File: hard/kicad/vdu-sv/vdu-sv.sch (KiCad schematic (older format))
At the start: 36 parts, among them J1 IOx, J2 (S)VGA, J3 IOx, U1 74HC138, U10 74HC245, U11 74HC245, U12 74HC245, U13 74HC574, U14 74HC157, U15 74HC86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

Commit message: first definitive placement
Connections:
- net D_BL: now also U10.12 (B6); no longer U10.11 (B7)
- net D_GH: now also U10.17 (B1); no longer U10.18 (B0)
- net D_RH: now also U10.18 (B0); no longer U10.17 (B1)
- net D_RL: now also U10.11 (B7); no longer U10.12 (B6)
- net I_BL: now also U10.8 (A6), U21.6; no longer U10.9 (A7), U21.11
- net I_GH: now also U10.3 (A1); no longer U10.2 (A0)
- net I_GL: now also U21.11; no longer U21.6
- net I_RH: now also U10.2 (A0); no longer U10.3 (A1)
- net I_RL: now also U10.9 (A7); no longer U10.8 (A6)
- net X_BL: now also U21.4; no longer U21.12
- net X_GL: now also U21.12; no longer U21.4
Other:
- moved on the sheet: R1, R2, R22, R23, U21B, U21D
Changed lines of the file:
@@
 L 74xx:74HC86 U21
 U 4 1 65C4FD1C
-P 7300 6100
-F 0 "U21" V 7325 6100 50  0000 C CNN
-F 1 "74HC86" V 7225 6100 50  0000 C CNN
-F 2 "Package_DIP:DIP-14_W7.62mm_Socket" H 7300 6100 50  0001 C CNN
-F 3 "http://www.ti.com/lit/gpn/sn74HC86" H 7300 6100 50  0001 C CNN
-	4    7300 6100
+P 6600 6100
+F 0 "U21" V 6625 6100 50  0000 C CNN
+F 1 "74HC86" V 6525 6100 50  0000 C CNN
+F 2 "Package_DIP:DIP-14_W7.62mm_Socket" H 6600 6100 50  0001 C CNN
+F 3 "http://www.ti.com/lit/gpn/sn74HC86" H 6600 6100 50  0001 C CNN
+	4    6600 6100
 	0    -1   -1   0
 $EndComp
@@
 L 74xx:74HC86 U21
 U 2 1 65C4FD30
-P 6600 6100
-F 0 "U21" V 6625 6100 50  0000 C CNN
-F 1 "74HC86" V 6525 6100 50  0000 C CNN
-F 2 "Package_DIP:DIP-14_W7.62mm_Socket" H 6600 6100 50  0001 C CNN
-F 3 "http://www.ti.com/lit/gpn/sn74HC86" H 6600 6100 50  0001 C CNN
-	2    6600 6100
-	0    -1   -1   0
-$EndComp
-Wire Wire Line
-	9100 5800 7300 5800
+P 7300 6100
+F 0 "U21" V 7325 6100 50  0000 C CNN
+F 1 "74HC86" V 7225 6100 50  0000 C CNN
+F 2 "Package_DIP:DIP-14_W7.62mm_Socket" H 7300 6100 50  0001 C CNN
+F 3 "http://www.ti.com/lit/gpn/sn74HC86" H 7300 6100 50  0001 C CNN
+	2    7300 6100
+	0    -1   -1   0
+$EndComp
 Wire Wire Line
 	6350 6400 6350 6425
@@
 	5850 6400 5850 6625
 Wire Wire Line
-	9100 5700 6950 5700
+	9100 5700 7300 5700
 Wire Wire Line
 	9100 5600 6600 5600
@@
 	9100 5300 7300 5300
 Wire Wire Line
-	9100 5200 6950 5200
-Wire Wire Line
-	9100 5100 6600 5100
+	9100 5200 6600 5200
+Wire Wire Line
+	9100 5100 6950 5100
 Wire Wire Line
 	10100 5800 10300 5800
@@
 L Device:R R23
 U 1 1 65F219EF
+P 10450 5700
+F 0 "R23" V 10400 5875 50  0000 C CNN
+F 1 "1K" V 10450 5700 50  0000 C CNN
+F 2 "Resistor_THT:R_Axial_DIN0207_L6.3mm_D2.5mm_P2.54mm_Vertical" V 10380 5700 50  0001 C CNN
+F 3 "~" H 10450 5700 50  0001 C CNN
+	1    10450 5700
+	0    1    1    0
+$EndComp
+$Comp
+L Device:R R22
+U 1 1 65F1EFAB
 P 10450 5800
-F 0 "R23" V 10400 5975 50  0000 C CNN
-F 1 "1K" V 10450 5800 50  0000 C CNN
+F 0 "R22" V 10400 5975 50  0000 C CNN
+F 1 "2K2" V 10450 5800 50  0000 C CNN
 F 2 "Resistor_THT:R_Axial_DIN0207_L6.3mm_D2.5mm_P2.54mm_Vertical" V 10380 5800 50  0001 C CNN
 F 3 "~" H 10450 5800 50  0001 C CNN
 	1    10450 5800
-	0    1    1    0
-$EndComp
-$Comp
-L Device:R R22
-U 1 1 65F1EFAB
-P 10450 5700
-F 0 "R22" V 10400 5875 50  0000 C CNN
-F 1 "2K2" V 10450 5700 50  0000 C CNN
-F 2 "Resistor_THT:R_Axial_DIN0207_L6.3mm_D2.5mm_P2.54mm_Vertical" V 10380 5700 50  0001 C CNN
-F 3 "~" H 10450 5700 50  0001 C CNN
-	1    10450 5700
 	0    1    1    0
 $EndComp
@@
 	0    1    1    0
 $EndComp
+Text Label 10125 5700 0    50   ~ 0
+D_BL
 Text Label 10125 5800 0    50   ~ 0
-D_BL
-Text Label 10125 5700 0    50   ~ 0
 D_RL
 Text Label 10125 5600 0    50   ~ 0
@@
 	10625 6400 10625 5900
 Wire Wire Line
-	10300 5200 10100 5200
+	10300 5100 10100 5100
 Wire Wire Line
 	10300 5300 10100 5300
 Text Label 10125 5300 0    50   ~ 0
 D_GM
-Text Label 10125 5200 0    50   ~ 0
+Text Label 10125 5100 0    50   ~ 0
 D_RH
 $Comp
@@
 L Device:R R1
 U 1 1 65AA0EB0
-P 10450 5200
-F 0 "R1" V 10400 5350 50  0000 C CNN
-F 1 "680" V 10450 5200 50  0000 C CIN
-F 2 "Resistor_THT:R_Axial_DIN0207_L6.3mm_D2.5mm_P2.54mm_Vertical" V 10380 5200 50  0001 C CNN
-F 3 "~" H 10450 5200 50  0001 C CNN
-	1    10450 5200
+P 10450 5100
+F 0 "R1" V 10400 5250 50  0000 C CNN
+F 1 "680" V 10450 5100 50  0000 C CIN
+F 2 "Resistor_THT:R_Axial_DIN0207_L6.3mm_D2.5mm_P2.54mm_Vertical" V 10380 5100 50  0001 C CNN
+F 3 "~" H 10450 5100 50  0001 C CNN
+	1    10450 5100
 	0    1    1    0
 $EndComp
@@
 	0    1    1    0
 $EndComp
-Text Label 10125 5100 0    50   ~ 0
+Text Label 10125 5200 0    50   ~ 0
 D_GH
 Wire Wire Line
-	10100 5100 10300 5100
+	10100 5200 10300 5200
 $Comp
 L Device:R R2
 U 1 1 65AA38B7
-P 10450 5100
-F 0 "R2" V 10400 5250 50  0000 C CNN
-F 1 "680" V 10450 5100 50  0000 C CNN
-F 2 "Resistor_THT:R_Axial_DIN0207_L6.3mm_D2.5mm_P2.54mm_Vertical" V 10380 5100 50  0001 C CNN
-F 3 "~" H 10450 5100 50  0001 C CNN
-	1    10450 5100
-	0    1    1    0
-$EndComp
-Wire Wire Line
-	10800 5800 10600 5800
-Wire Wire Line
-	10600 5700 10700 5700
+P 10450 5200
+F 0 "R2" V 10400 5350 50  0000 C CNN
+F 1 "680" V 10450 5200 50  0000 C CNN
+F 2 "Resistor_THT:R_Axial_DIN0207_L6.3mm_D2.5mm_P2.54mm_Vertical" V 10380 5200 50  0001 C CNN
+F 3 "~" H 10450 5200 50  0001 C CNN
+	1    10450 5200
+	0    1    1    0
+$EndComp
 Wire Wire Line
 	10600 5600 10750 5600
@@
 	10600 5300 10750 5300
 Wire Wire Line
-	10600 5200 10700 5200
-Wire Wire Line
 	10700 5000 10900 5000
 Wire Wire Line
 	10800 5200 10900 5200
 Wire Wire Line
-	10800 5400 10800 5800
-Connection ~ 10800 5400
-Wire Wire Line
 	10800 5400 10800 5200
 Wire Wire Line
-	10700 5700 10700 5500
-Connection ~ 10700 5500
-Wire Wire Line
-	10700 5500 10700 5200
-Wire Wire Line
 	10750 5600 10750 5300
-Wire Wire Line
-	10750 5100 10900 5100
-Wire Wire Line
-	10600 5100 10750 5100
-Connection ~ 10750 5100
 Connection ~ 10750 5300
 Wire Wire Line
-	10750 5300 10750 5100
-Connection ~ 10700 5200
-Wire Wire Line
-	10700 5200 10700 5000
-Wire Wire Line
-	6950 5700 6950 5800
+	10750 5300 10750 5200
 Wire Wire Line
 	6600 5600 6600 5800
@@
 	6250 5500 6250 5800
 Wire Wire Line
-	6600 5100 6600 4925
-Wire Wire Line
-	6950 4925 6950 5200
-Wire Wire Line
 	7300 5300 7300 4925
 Wire Wire Line
 	7650 4925 7650 5400
+Text Label 9100 5700 2    50   ~ 0
+I_BL
 Text Label 9100 5800 2    50   ~ 0
-I_BL
-Text Label 9100 5700 2    50   ~ 0
 I_RL
 Text Label 9100 5600 2    50   ~ 0
@@
 Text Label 9100 5400 2    50   ~ 0
 I_BH
+Text Label 9100 5100 2    50   ~ 0
+I_RH
 Text Label 9100 5200 2    50   ~ 0
-I_RH
-Text Label 9100 5100 2    50   ~ 0
 I_GH
 $Comp
@@
 	1    0    0    1
 $EndComp
+Wire Wire Line
+	10800 5400 10800 5700
+Wire Wire Line
+	10600 5700 10800 5700
+Connection ~ 10800 5400
+Wire Wire Line
+	10700 5500 10700 5800
+Connection ~ 10700 5500
+Wire Wire Line
+	10700 5800 10600 5800
+Wire Wire Line
+	7300 5700 7300 5800
+Wire Wire Line
+	6950 5800 6950 5750
+Wire Wire Line
+	6950 5750 7800 5750
+Wire Wire Line
+	7800 5750 7800 5800
+Wire Wire Line
+	7800 5800 9100 5800
+Wire Wire Line
+	10700 5000 10700 5100
+Wire Wire Line
+	10600 5200 10750 5200
+Connection ~ 10750 5200
+Wire Wire Line
+	10750 5200 10750 5100
+Wire Wire Line
+	10750 5100 10900 5100
+Wire Wire Line
+	10600 5100 10700 5100
+Connection ~ 10700 5100
+Wire Wire Line
+	10700 5100 10700 5500
+Wire Wire Line
+	6950 5100 6950 4925
+Wire Wire Line
+	6600 5200 6600 4925
 $EndSCHEMATC

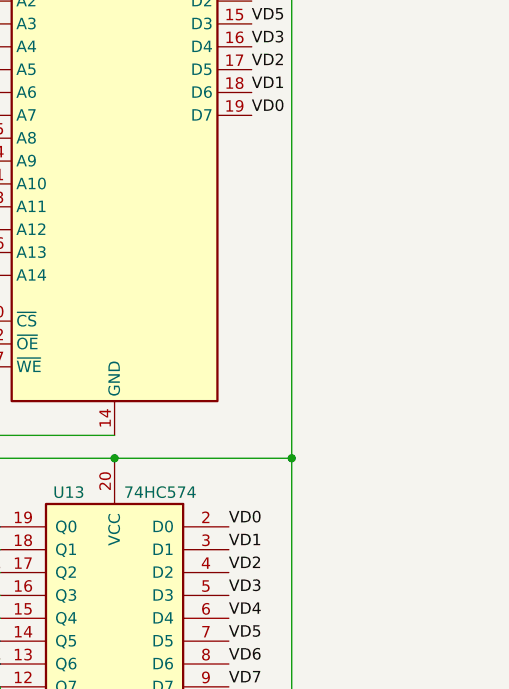
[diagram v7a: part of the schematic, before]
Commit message: contour and mounting holes
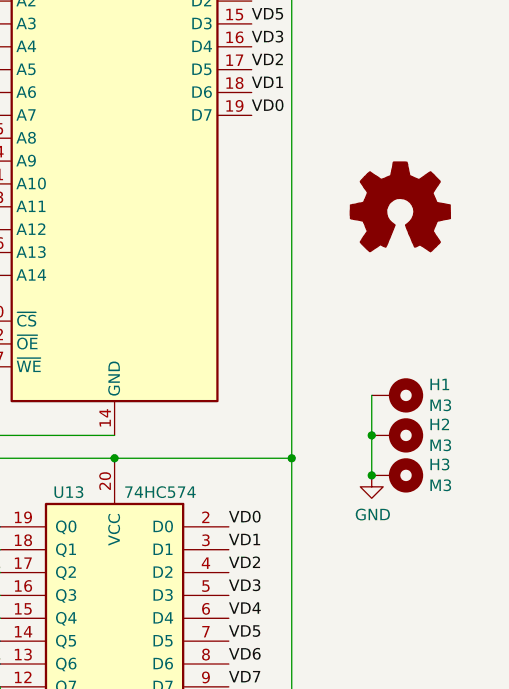
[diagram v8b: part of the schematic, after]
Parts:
- added H1, H2, H3: M3, MountingHole:MountingHole_3.2mm_M3_DIN965_Pad, symbol Mechanical:MountingHole_Pad
- added LOGO1: La Jaquería, durango:jaqueria, symbol Graphic:Logo_Open_Hardware_Small
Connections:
- net GND: now also H1.1, H2.1, H3.1
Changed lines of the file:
@@
 Wire Wire Line
 	6600 5200 6600 4925
+$Comp
+L Mechanical:MountingHole_Pad H1
+U 1 1 65AC552F
+P 10850 2800
+F 0 "H1" V 10804 2950 50  0000 L CNN
+F 1 "M3" V 10895 2950 50  0000 L CNN
+F 2 "MountingHole:MountingHole_3.2mm_M3_DIN965_Pad" H 10850 2800 50  0001 C CNN
+F 3 "~" H 10850 2800 50  0001 C CNN
+	1    10850 2800
+	0    1    1    0
+$EndComp
+$Comp
+L Mechanical:MountingHole_Pad H2
+U 1 1 65ADC50B
+P 10850 2975
+F 0 "H2" V 10804 3125 50  0000 L CNN
+F 1 "M3" V 10895 3125 50  0000 L CNN
+F 2 "MountingHole:MountingHole_3.2mm_M3_DIN965_Pad" H 10850 2975 50  0001 C CNN
+F 3 "~" H 10850 2975 50  0001 C CNN
+	1    10850 2975
+	0    1    1    0
+$EndComp
+$Comp
+L Mechanical:MountingHole_Pad H3
+U 1 1 65ADDD4B
+P 10850 3150
+F 0 "H3" V 10804 3300 50  0000 L CNN
+F 1 "M3" V 10895 3300 50  0000 L CNN
+F 2 "MountingHole:MountingHole_3.2mm_M3_DIN965_Pad" H 10850 3150 50  0001 C CNN
+F 3 "~" H 10850 3150 50  0001 C CNN
+	1    10850 3150
+	0    1    1    0
+$EndComp
+Connection ~ 10750 2975
+Wire Wire Line
+	10750 2975 10750 3150
+$Comp
+L power:GND #PWR0116
+U 1 1 65AF2BC5
+P 10750 3150
+F 0 "#PWR0116" H 10750 2900 50  0001 C CNN
+F 1 "GND" H 10755 2977 50  0000 C CNN
+F 2 "" H 10750 3150 50  0001 C CNN
+F 3 "" H 10750 3150 50  0001 C CNN
+	1    10750 3150
+	1    0    0    -1
+$EndComp
+$Comp
+L Graphic:Logo_Open_Hardware_Small LOGO1
+U 1 1 65AF78F3
+P 10875 2000
+F 0 "LOGO1" H 10875 2275 50  0001 C CNN
+F 1 "La Jaquería" H 10875 1775 50  0001 C CNN
+F 2 "durango:jaqueria" H 10875 2000 50  0001 C CNN
+F 3 "~" H 10875 2000 50  0001 C CNN
+	1    10875 2000
+	1    0    0    -1
+$EndComp
+Connection ~ 10750 3150
+Wire Wire Line
+	10750 2800 10750 2975
 $EndSCHEMATC
